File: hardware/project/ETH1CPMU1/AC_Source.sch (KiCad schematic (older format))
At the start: 106 parts, among them K801 TQ2SA-5V, U801 AD5453YRMZ, U802 LT1468, U803 LT1468, U804 AD9835, U805 ECS-3225SMV-500-GP-TR, U806 74AHCT1G08, U807 REF192, U808 TL071, U809 DG408DY, U810 TL072, U811 ADS7818, U812 AD5689BRUZ, U813 TL071, U814 TL072, U815 TXB0104D

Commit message: Schematic design
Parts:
- renumbered C801 to C1301, C802 to C1302, C803 to C1303, C804 to C1304, C805 to C1305, C806 to C1306, C807 to C1307, C808 to C1308, C809 to C1309, C810 to C1310, C811 to C1311, C812 to C1312, C813 to C1313, C815 to C1314, C816 to C1315, C819 to C1316, C820 to C1317, C814 to C1318, C817 to C1319, C818 to C1320, C821 to C1321, C822 to C1322, C823 to C1323, C824 to C1324, C826 to C1325, C828 to C1326, C825 to C1327, C827 to C1328, C829 to C1329, C830 to C1330, C831 to C1331, C832 to C1332, C833 to C1333, C834 to C1334, C835 to C1335, C836 to C1336, C837 to C1337, C838 to C1338, C839 to C1339, C840 to C1340, C841 to C1341, C842 to C1342, D801 to D1301, D802 to D1302, K801 to K1301, L801 to L1301, L802 to L1302, L803 to L1303, R801 to R1301, R802 to R1302, R803 to R1303, R804 to R1304, R805 to R1305, R806 to R1306, R807 to R1307, R808 to R1308, R809 to R1309, R810 to R1310, R811 to R1311, R839 to R1312, R812 to R1313, R814 to R1314, R815 to R1315, R816 to R1316, R817 to R1317, R838 to R1318, R813 to R1319, R824 to R1320, R825 to R1321, R826 to R1322, R818 to R1323, R819 to R1324, R820 to R1325, R821 to R1326, R822 to R1327, R840 to R1328, R829 to R1329, R823 to R1330, R827 to R1331, R841 to R1332, R828 to R1333, R831 to R1334, R842 to R1335, R833 to R1336, R834 to R1337, R835 to R1338, R843 to R1339, R836 to R1340, R837 to R1341, R830 to R1342, R832 to R1343, U801 to U1301, U802 to U1302, U803 to U1303, U804 to U1304, U805 to U1305, U806 to U1306, U815 to U1307, U807 to U1308, U808 to U1309, U809 to U1310, U810 to U1311, U811 to U1312, U812 to U1313, U813 to U1314, U814 to U1315

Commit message: PCB design.
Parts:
- removed U1309, U1314: TL071, Package_SO:SOIC-8_3.9x4.9mm_P1.27mm, symbol Amplifier_Operational:TL071
- added unit 1 of U1309
- added unit 2 of U1311
- added unit 3 of U1314
- renumbered U1311 to U1309, U1315 to U1311, U1315 to U1314
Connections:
- net labels removed: +3.3VF
- wire segments 371 -> 372
- no-connect marks 17 -> 13
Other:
- moved on the sheet: U1311A

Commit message: PCB design
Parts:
- added C1343: 100n, Capacitor_SMD:C_0603_1608Metric_Pad1.05x0.95mm_HandSolder, symbol Device:C
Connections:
- net -15VF: now also C1343.1
- net AGNDF: now also C1343.2
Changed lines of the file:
@@
 Wire Wire Line
 	10450 9950 10450 9900
+$Comp
+L Device:C C1343
+U 1 1 5DE7325A
+P 11100 10250
+F 0 "C1343" H 11215 10296 50  0000 L CNN
+F 1 "100n" H 11215 10205 50  0000 L CNN
+F 2 "Capacitor_SMD:C_0603_1608Metric_Pad1.05x0.95mm_HandSolder" H 11138 10100 50  0001 C CNN
+F 3 "~" H 11100 10250 50  0001 C CNN
+	1    11100 10250
+	1    0    0    -1
+$EndComp
+$Comp
+L ETH1CPMU1:AGNDF #PWR01400
+U 1 1 5DE73260
+P 11100 10600
+F 0 "#PWR01400" H 11100 10350 50  0001 C CNN
+F 1 "AGNDF" H 11105 10427 50  0000 C CNN
+F 2 "" H 11100 10600 50  0001 C CNN
+F 3 "" H 11100 10600 50  0001 C CNN
+	1    11100 10600
+	1    0    0    -1
+$EndComp
+Wire Wire Line
+	11100 10600 11100 10400
+Wire Wire Line
+	11100 10100 11100 9900
+$Comp
+L ETH1CPMU1:-15VF #PWR01399
+U 1 1 5DE73268
+P 11100 9900
+F 0 "#PWR01399" H 11100 9750 50  0001 C CNN
+F 1 "-15VF" H 11115 10073 50  0000 C CNN
+F 2 "" H 11100 9900 50  0001 C CNN
+F 3 "" H 11100 9900 50  0001 C CNN
+	1    11100 9900
+	1    0    0    -1
+$EndComp
 $EndSCHEMATC

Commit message: PCB design
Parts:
- added C1242: 10p, Capacitor_SMD:C_0603_1608Metric_Pad1.05x0.95mm_HandSolder, symbol Device:C
- added Q1201: BC847, Package_TO_SOT_SMD:SOT-23, symbol Transistor_BJT:BC847
- added R1241: 10k, Resistor_SMD:R_0603_1608Metric_Pad1.05x0.95mm_HandSolder, symbol Device:R
- U1206: renamed from U1311; footprint (none) -> Package_SO:SOIC-8_3.9x4.9mm_P1.27mm
- U1207: renamed from U1309; footprint (none) -> Package_SO:SOIC-8_3.9x4.9mm_P1.27mm
- U1211: renamed from U1314; footprint (none) -> Package_SO:SOIC-8_3.9x4.9mm_P1.27mm
- renumbered C1329 to C1201, C1314 to C1202, C1330 to C1203, C1331 to C1204, C1315 to C1205, C1332 to C1206, C1333 to C1207, C1334 to C1208, C1335 to C1209, C1316 to C1210, C1325 to C1211, C1336 to C1212, C1317 to C1213, C1304 to C1214, C1337 to C1215, C1313 to C1216, C1326 to C1217, C1338 to C1218, C1309 to C1219, C1305 to C1220, C1310 to C1221, C1306 to C1222, C1311 to C1223, C1307 to C1224, C1312 to C1225, C1339 to C1226, C1340 to C1227, C1308 to C1228, C1341 to C1229, C1327 to C1230, C1342 to C1231, C1303 to C1232, C1321 to C1233, C1343 to C1234, C1322 to C1235, C1319 to C1236, C1320 to C1237, C1328 to C1238, C1301 to C1239, C1323 to C1240, C1324 to C1241, C1318 to C1243, C1302 to C1244, D1302 to D1201, D1301 to D1202, K1301 to K1201, L1301 to L1201, L1302 to L1202, L1303 to L1203, R1320 to R1201, R1338 to R1202, R1334 to R1203, R1340 to R1204, R1321 to R1205, R1311 to R1206, R1313 to R1207, R1314 to R1208, R1305 to R1209, R1315 to R1210, R1316 to R1211, R1329 to R1212, R1310 to R1213, R1336 to R1214, R1341 to R1215, R1337 to R1216, R1308 to R1217, R1317 to R1218, R1322 to R1219, R1328 to R1220, R1332 to R1221, R1309 to R1222, R1339 to R1223, R1318 to R1224, R1335 to R1225, R1306 to R1226, R1333 to R1227, R1312 to R1228, R1331 to R1229, R1342 to R1230, R1303 to R1231, R1325 to R1232, R1343 to R1233, R1330 to R1234, R1326 to R1235, R1301 to R1236, R1307 to R1237, R1327 to R1238, R1304 to R1239, R1323 to R1240, R1302 to R1242, R1319 to R1243, R1324 to R1244, U1305 to U1201, U1308 to U1202, U1306 to U1203, U1313 to U1204, U1304 to U1205, U1311 to U1206, U1309 to U1207, U1307 to U1208, U1310 to U1209, U1301 to U1210, U1314 to U1211, U1302 to U1212, U1303 to U1213, U1312 to U1214
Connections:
- net AC_RELAY: now also Q1201.3 (C), R1241.1
- net DGNDF: now also C1242.2, Q1201.2 (E)
- new net: C1242.1, Q1201.1 (B), R1241.2

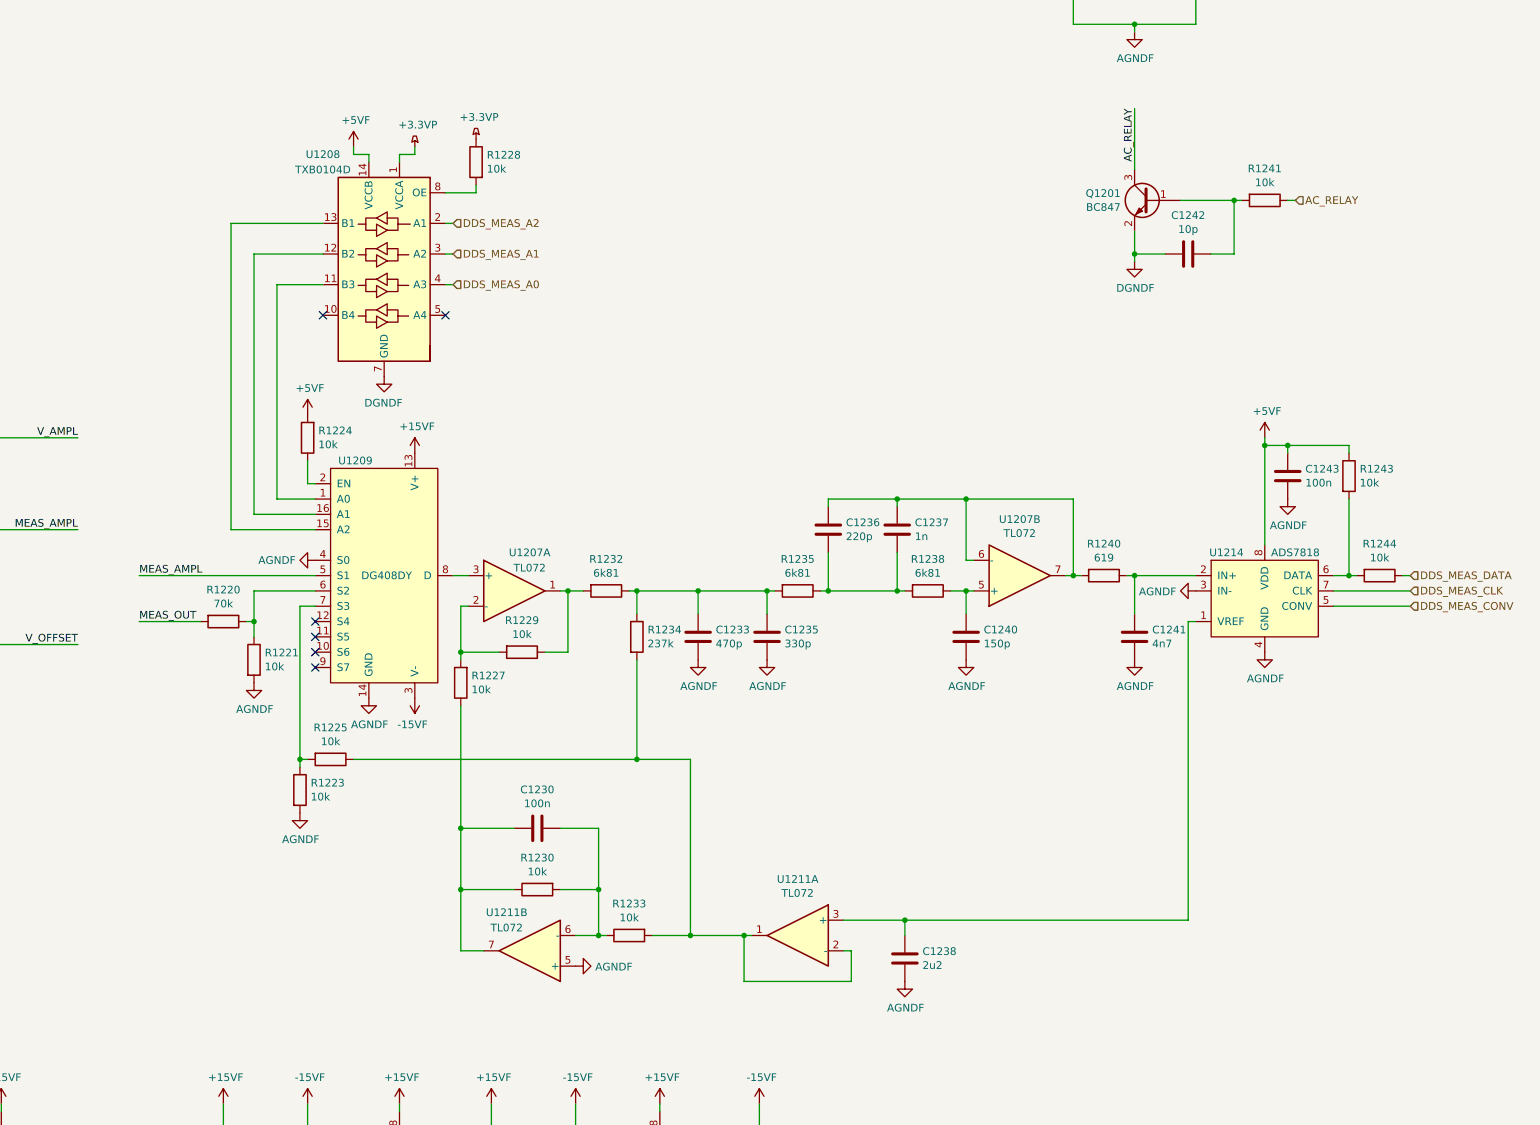
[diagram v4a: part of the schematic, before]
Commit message: Changed distances for fills and added voltage level IC.
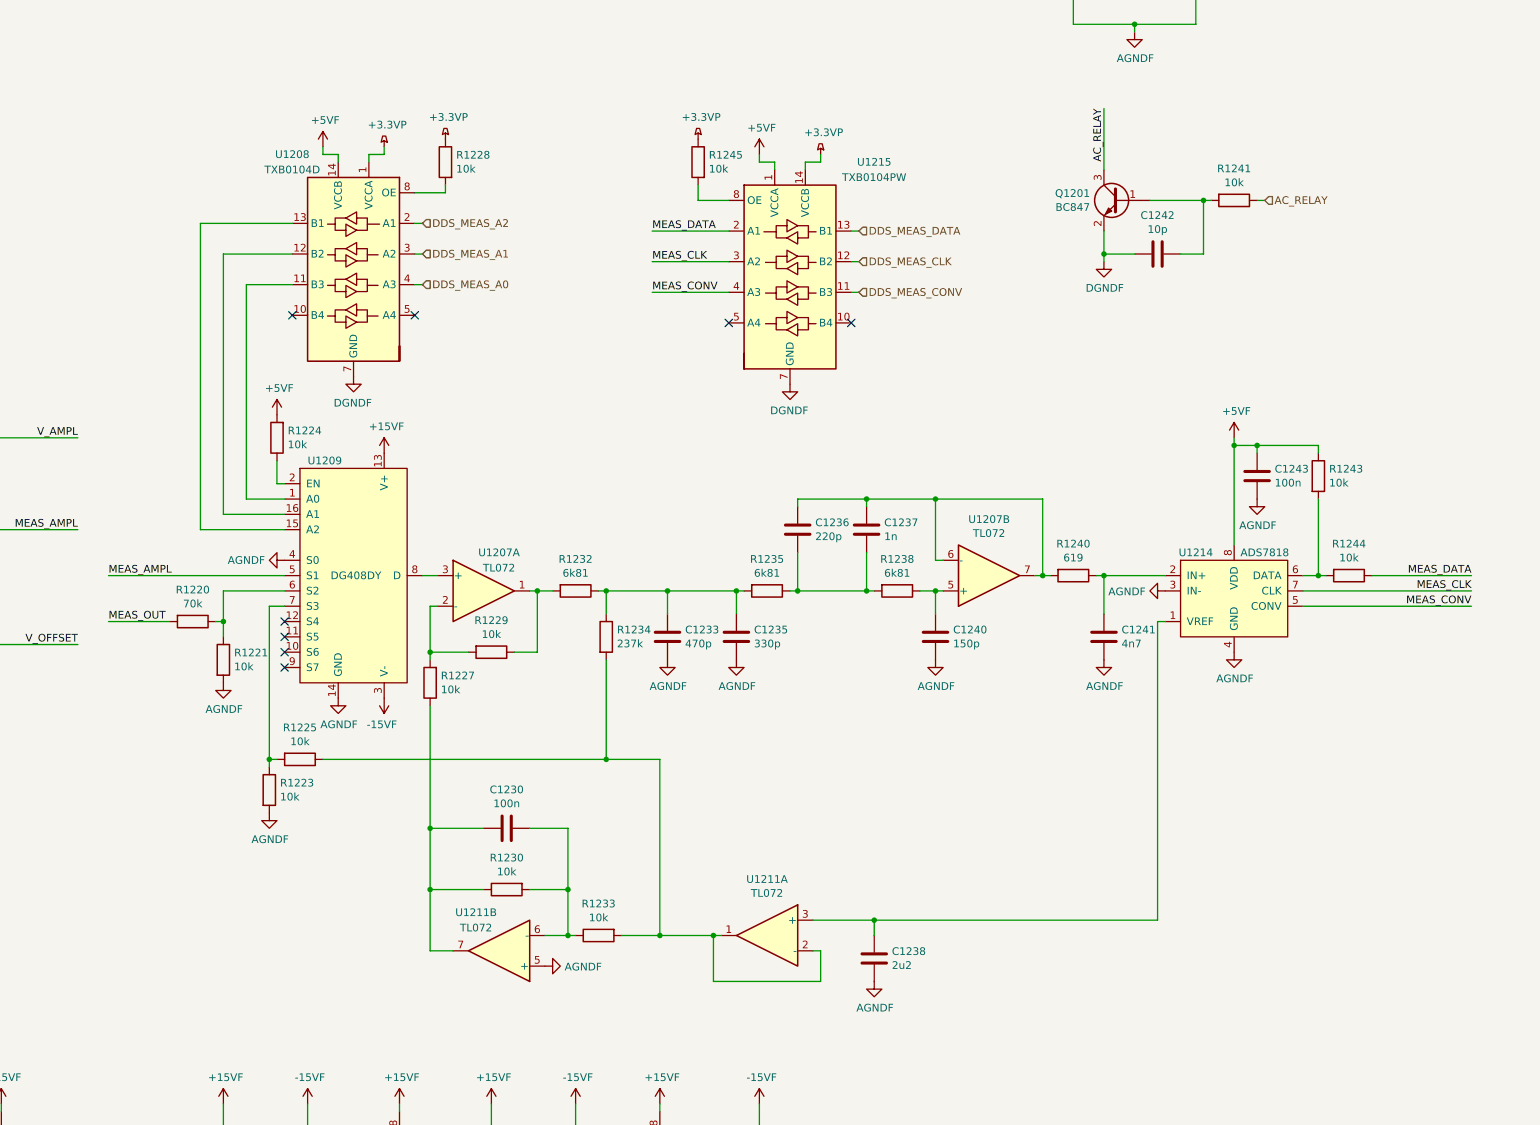
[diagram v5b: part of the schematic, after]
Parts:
- added R1245: 10k, Resistor_SMD:R_0603_1608Metric_Pad1.05x0.95mm_HandSolder, symbol Device:R
- added U1215: TXB0104PW, Package_SO:TSSOP-14_4.4x5mm_P0.65mm, symbol Logic_LevelTranslator:TXB0104PW
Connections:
- net +3.3VP: now also R1245.1, U1215.14 (VCCB)
- net +5VF: now also U1215.1 (VCCA)
- net DDS_MEAS_CLK: now also U1215.12 (B2); no longer U1214.7 (CLK)
- net DDS_MEAS_CONV: now also U1215.11 (B3); no longer U1214.5 (CONV)
- net DDS_MEAS_DATA: now also U1215.13 (B1); no longer R1244.1
- net DGNDF: now also U1215.7 (GND)
- new net: R1245.2, U1215.8 (OE)
- new net MEAS_CLK: U1214.7 (CLK), U1215.3 (A2)
- new net MEAS_CONV: U1214.5 (CONV), U1215.4 (A3)
- new net MEAS_DATA: R1244.1, U1215.2 (A1)
- no-connect marks 13 -> 15
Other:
- moved on the sheet: C1230, C1233, C1235, C1236, C1237, C1238, C1240, C1241, C1242, C1243, Q1201, R1220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

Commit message: Added summing op amp.
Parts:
- removed U1208: TXB0104D, Package_SO:SOIC-14_3.9x8.7mm_P1.27mm, symbol Logic_LevelTranslator:TXB0104D
- added R1246, R1247: 1k, Resistor_SMD:R_0603_1608Metric_Pad1.05x0.95mm_HandSolder, symbol Device:R
- added U1208: TXB0104PW, Package_SO:TSSOP-14_4.4x5mm_P0.65mm, symbol Logic_LevelTranslator:TXB0104PW
- added U1216: LT1468, Package_SO:SSOP-8_3.9x5.05mm_P1.27mm, symbol ETH1CPMU1:LT1468
- R1236, R1237: value R -> 1k
- R1239: value R -> 10k
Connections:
- net +15VF: now also U1216.7 (V+)
- net +3.3VP: now also U1215.1 (VCCA), U1208.1 (VCCA); no longer U1215.14 (VCCB)
- net +5VF: now also U1215.14 (VCCB), U1208.14 (VCCB); no longer U1215.1 (VCCA)
- net -15VF: now also U1216.4 (V-)
- net AGNDF: now also U1216.3 (+)
- net DDS_MEAS_A0: now also U1208.4 (A3)
- net DDS_MEAS_A1: now also U1208.3 (A2)
- net DDS_MEAS_A2: now also U1208.2 (A1)
- net DDS_MEAS_CLK: now also U1215.3 (A2); no longer U1215.12 (B2)
- net DDS_MEAS_CONV: now also U1215.4 (A3); no longer U1215.11 (B3)
- net DDS_MEAS_DATA: now also U1215.2 (A1); no longer U1215.13 (B1)
- net DGNDF: now also U1208.7 (GND)
- net MEAS_CLK: now also U1215.12 (B2); no longer U1215.3 (A2)
- net MEAS_CONV: now also U1215.11 (B3); no longer U1215.4 (A3)
- net MEAS_DATA: now also U1215.13 (B1); no longer U1215.2 (A1)
- net V_OFFSET: now also R1246.2; no longer R1236.2
- net at C1239.2, R1237.1, R1239.2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: no longer R1236.1
- net at C1239.1, R1239.1, U1213.6: now also R1236.2; no longer K1201.3
- net at U1209.1 (A0): now also U1208.11 (B3)
- net at U1209.15 (A2): now also U1208.13 (B1)
- net at U1209.16 (A1): now also U1208.12 (B2)
- net at R1228.2: now also U1208.8 (OE)
- new net: K1201.3, R1247.1, U1216.6
- new net: R1236.1, R1246.1, R1247.2, U1216.2 (-)
- no-connect marks 15 -> 17
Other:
- moved on the sheet: C1214, C1216, C1219, C1220, C1221, C1222, C1223, C1224, C1225, C1228, C1232, C1239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
